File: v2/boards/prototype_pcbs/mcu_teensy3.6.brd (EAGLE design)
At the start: 27.6 x 72.2 mm, 9 parts, among them Q1 BS108, U1 TEENSY3_6, U2 MCP101

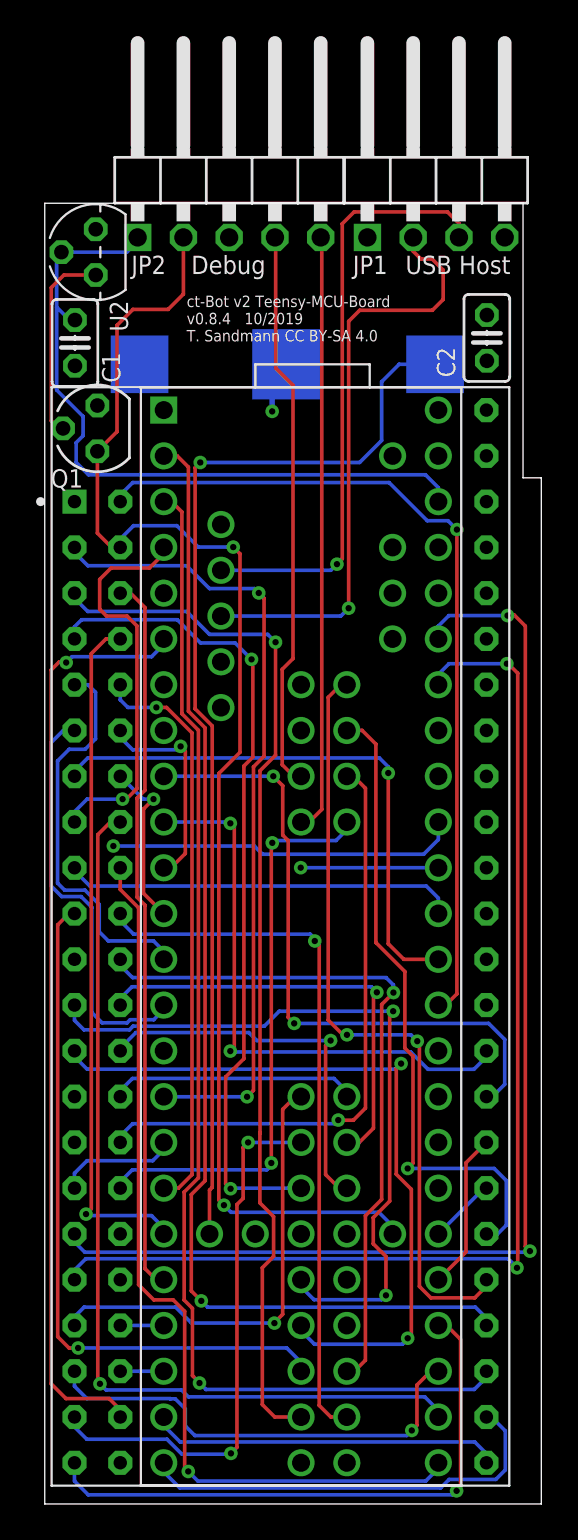
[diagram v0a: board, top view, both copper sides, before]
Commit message: folder structure cleanup, 3d model: base updated
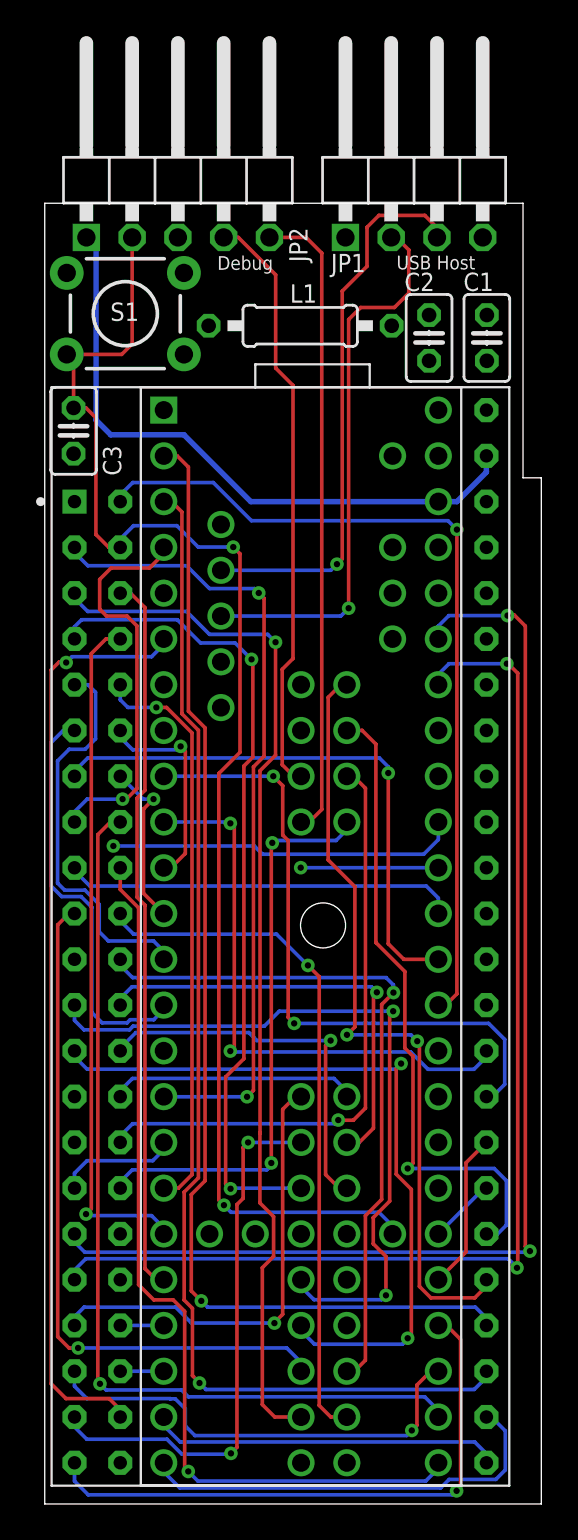
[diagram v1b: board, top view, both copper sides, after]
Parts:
- removed BAT1: RTC Bat, adafruit:CR1220-SMD
- removed Q1: BS108, ct-bot:SOT54E
- removed U2: MCP101, ct-bot:TO-92
- added C3: 1nF, rcl:C025-025X050
- added L1: 10uH, rcl:0207/10
- added S1: RESET, SparkFun-Switches:TACTILE_SWITCH_PTH_6.0MM
- moved C1 22.9 mm to (24.5, 64.7), turned to 90 degrees
- moved C2 3.21 mm to (21.3, 64.7), turned to 270 degrees
- moved JP2 2.84 mm to (7.39, 74.1)
- moved JP1 1.22 mm to (20.5, 74.1)
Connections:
- removed net N$1: Q1.G, U2.1
- removed net VBAT_RTC: BAT1.+$1, U1.VBAT
- new net +3V3: C2.1, L1.2, ST1.45
- new net AREF: L1.1, U1.AREF
- net +5V: now also C1.1; no longer C2.1
- net 3V3_TEENSY: now also ST1.46; no longer C1.1, U2.2
- net AGND: now also C2.2
- net GND: now also C3.2, S1.1; no longer BAT1.-, C2.2, Q1.S, U2.3
- net RESET: now also C3.1, S1.3; no longer Q1.D
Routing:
- net VBAT_RTC: track 60.6 -> 0.00 mm, vias 1 -> 0
- net AREF: track 0.00 -> 21.5 mm
- net N$1: track 11.0 -> 0.00 mm
- net +3V3: track 0.00 -> 10.2 mm
- net AGND: track 0.00 -> 6.89 mm
- net 3V3_TEENSY: track 40.0 -> 35.5 mm
- net GND: track 2.96 -> 0.00 mm, vias 1 -> 0
- net USB1_D_P: track 33.4 -> 30.9 mm
- net USB1_D_N: track 33.4 -> 30.9 mm
- net SWDIO: track 33.2 -> 35.6 mm
- net +5V: track 40.8 -> 43.1 mm
- net SWDCLK: track 31.2 -> 32.9 mm
- net RESET: track 76.2 -> 77.6 mm
- net RX6: track 39.4 -> 38.3 mm
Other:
- board text added: "ct-Bot v2 Teensy-MCU-Board v0.8.5 12/2019 T. Sandmann CC BY-SA 4.0"
- board text removed: "ct-Bot v2 Teensy-MCU-Board v0.8.4 10/2019 T. Sandmann CC BY-SA 4.0"
